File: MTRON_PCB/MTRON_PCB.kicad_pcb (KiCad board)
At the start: 2 copper layers, 48 x 50 mm, 42 parts, among them J1 Conn_01x02, J2 Conn_01x02, J3 Conn_01x02, J4 Conn_01x02, J5 Conn_01x06, J6 Conn_01x02, J7 Conn_01x03, J8 Conn_01x02, J9 Conn_01x03, U1 Teensy4.0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

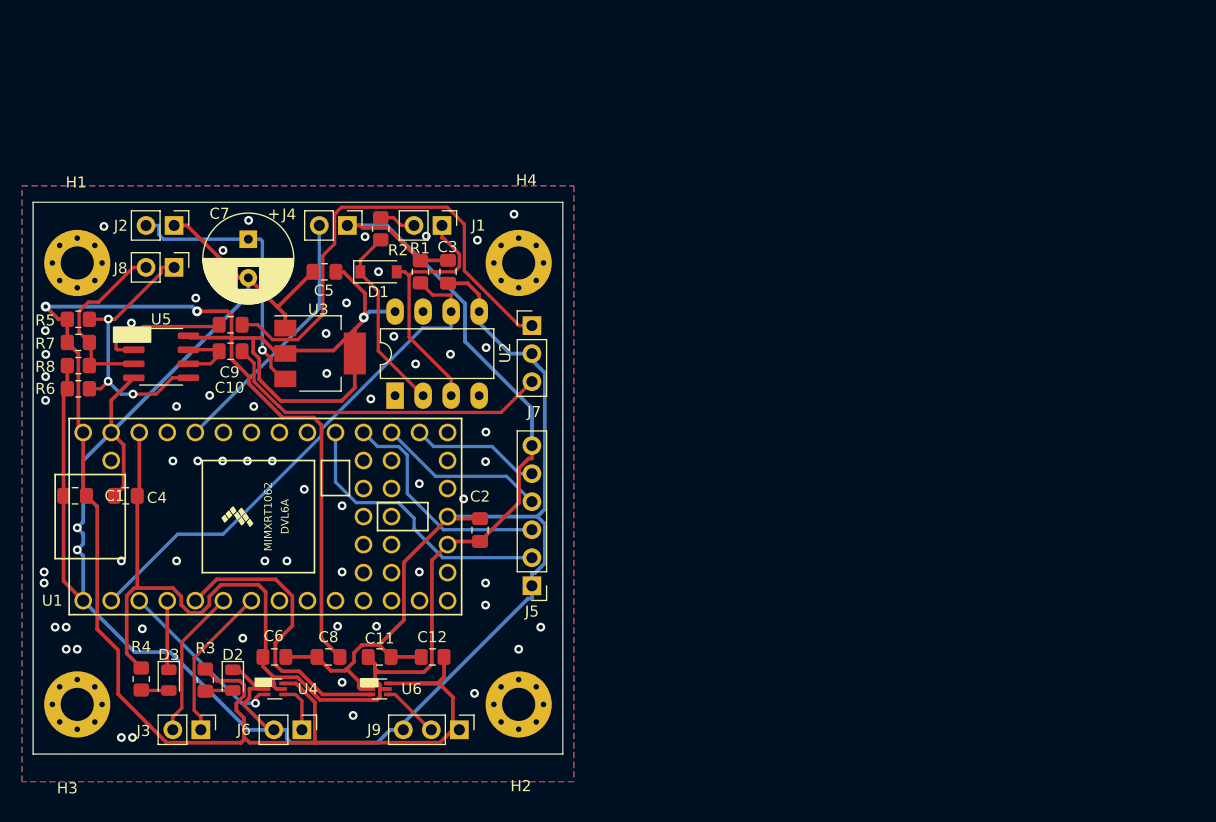
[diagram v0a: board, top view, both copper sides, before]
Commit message: update design files, new version has less parts
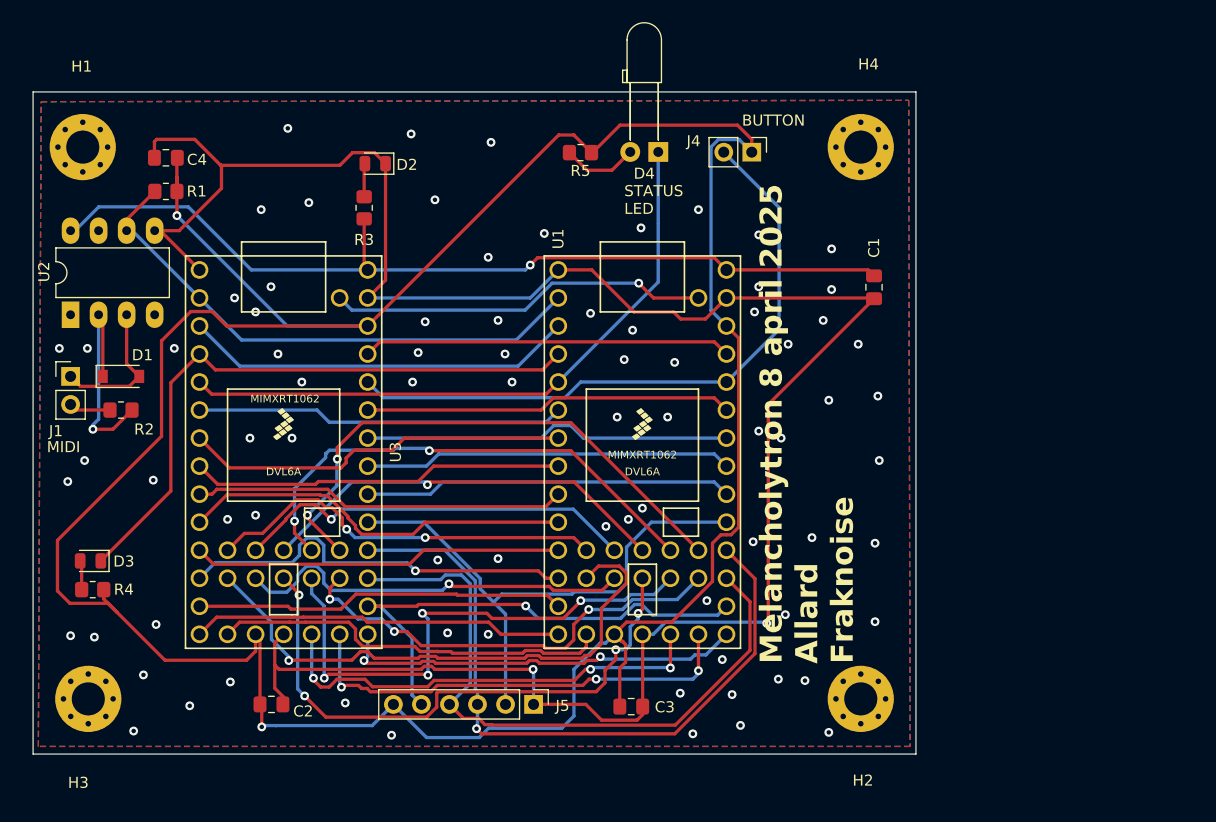
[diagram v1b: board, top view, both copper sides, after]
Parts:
- removed C10, C9: 2u2, Capacitor_SMD:C_0805_2012Metric_Pad1.18x1.45mm_HandSolder
- removed C11, C12, C5, C6, C8: 100n, Capacitor_SMD:C_0805_2012Metric_Pad1.18x1.45mm_HandSolder
- removed C7: 330uF/35V, Capacitor_THT:CP_Radial_D8.0mm_P3.50mm
- removed J2, J3, J6, J8: Conn_01x02, Connector_PinHeader_2.54mm:PinHeader_1x02_P2.54mm_Vertical
- removed J7, J9: Conn_01x03, Connector_PinHeader_2.54mm:PinHeader_1x03_P2.54mm_Vertical
- removed R6, R7, R8: 47k, Resistor_SMD:R_0805_2012Metric_Pad1.20x1.40mm_HandSolder
- removed U4, U6: SN74LVC1T45DRL, Package_TO_SOT_SMD:SOT-563
- removed U5: LM358, Package_SO:SOIC-8_3.9x4.9mm_P1.27mm
- added D4: LED, LED_THT:LED_D3.0mm_Horizontal_O6.35mm_Z6.0mm, F.Cu at (173.7, 60.9)
- R5: value 47k -> 470R
- U3: value AZ1117-5.0 -> Teensy4.0; footprint Package_TO_SOT_SMD:SOT-223-3_TabPin2 -> TeensyLibrary:Teensy40
- moved C1 74.8 mm to (193.2, 73.2), turned to -90 degrees
- moved D2 48.5 mm to (148.0, 62.0), turned to 180 degrees
- moved R5 47.9 mm to (166.6, 61.0), turned to 180 degrees
- moved R3 45.2 mm to (147.0, 66.0), turned to 90 degrees
- moved C3 42.8 mm to (171.2, 111.2), turned to 0 degrees
- moved J4 37.2 mm to (182.1, 61.0)
- moved J1 36.3 mm to (120.4, 81.3), turned to 0 degrees
- moved U1 34.7 mm to (172.2, 88.1), turned to -90 degrees
- moved H4 32.7 mm to (192.0, 60.5)
- moved H2 31.0 mm to (192.0, 110.5)
- moved C4 30.8 mm to (129.0, 61.5)
- moved U2 30.3 mm to (120.4, 75.7)
- moved R2 28.7 mm to (125.0, 84.3), turned to 0 degrees
- moved D1 25.2 mm to (125.0, 81.3)
- moved C2 24.6 mm to (138.6, 111.0), turned to 0 degrees
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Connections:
- C1 pad 1: +5V -> P33
- C1 pad 2: GND -> P1
- C2 pad 1: +3V3 -> P16
- C2 pad 2: GND -> P1
- C3 pad 1: +3V3 -> P16
- C3 pad 2: GND -> P1
- C4 pad 1: +3V3 -> P16
- C4 pad 2: GND -> P1
- D2 pad 1: GND -> P1
- J4 pad 1: +3V3 -> P16
- J4 pad 2: Net-(J4-Pin_2) -> P29
- J5 pad 1: GND -> P1
- J5 pad 2: Net-(J5-Pin_2) -> P24
- J5 pad 3: Net-(J5-Pin_3) -> P23
- J5 pad 4: Net-(J5-Pin_4) -> P22
- J5 pad 5: Net-(J5-Pin_5) -> P21
- J5 pad 6: +3V3 -> P16
- R1 pad 1: +3V3 -> P16
- R1 pad 2: Net-(U1-0_RX1_CRX2_CS1) -> P2
- R3 pad 1: +5V -> P33
- R4 pad 1: +3V3 -> P16
- R5 pad 1: +5V -> P16
- U1 pad 1: GND -> P1
- U1 pad 10: unconnected-(U1-8_TX2_IN1) -> P10
- U1 pad 11: unconnected-(U1-9_OUT1C) -> P11
- U1 pad 12: unconnected-(U1-10_CS_MQSR) -> P12
- U1 pad 13: unconnected-(U1-11_MOSI_CTX1) -> P13
- U1 pad 14: unconnected-(U1-12_MISO_MQSL) -> P14
- U1 pad 15: unconnected-(U1-VBAT) -> P15
- U1 pad 16: +3V3 -> P16
- U1 pad 17: GND -> P1
- U1 pad 18: unconnected-(U1-PROGRAM) -> P18
- U1 pad 19: unconnected-(U1-ON_OFF) -> P19
- U1 pad 2: Net-(U1-0_RX1_CRX2_CS1) -> P2
- U1 pad 20: unconnected-(U1-13_SCK_CRX1_LED) -> P20
- U1 pad 21: Net-(J5-Pin_5) -> P21
- U1 pad 22: Net-(J5-Pin_4) -> P22
- U1 pad 23: Net-(J5-Pin_3) -> P23
- U1 pad 24: Net-(J5-Pin_2) -> P24
- U1 pad 25: unconnected-(U1-18_A4_SDA0) -> P25
- U1 pad 26: unconnected-(U1-19_A5_SCL0) -> P26
- U1 pad 27: unconnected-(U1-20_A6_TX5_LRCLK1) -> P27
- U1 pad 28: unconnected-(U1-21_A7_RX5_BCLK1) -> P28
- U1 pad 29: Net-(J4-Pin_2) -> P29
- U1 pad 3: Net-(U1-1_TX1_CTX2_MISO1) -> P3
- U1 pad 30: unconnected-(U1-23_A9_CRX1_MCLK1) -> P30
- U1 pad 31: +3V3 -> P16
- U1 pad 32: GND -> P1
- U1 pad 33: +5V -> P33
- U1 pad 34: unconnected-(U1-VUSB) -> P34
- U1 pad 35: unconnected-(U1-24_A10_TX6_SCL2) -> P35
- U1 pad 36: unconnected-(U1-25_A11_RX6_SDA2) -> P36
- U1 pad 37: unconnected-(U1-26_A12_MOSI1) -> P37
- U1 pad 38: unconnected-(U1-27_A13_SCK1) -> P38
- U1 pad 39: unconnected-(U1-28_RX7) -> P39
- U1 pad 40: unconnected-(U1-29_TX7) -> P40
- U1 pad 41: unconnected-(U1-30_CRX3) -> P41
- U1 pad 42: unconnected-(U1-31_CTX3) -> P42
- U1 pad 43: unconnected-(U1-32_OUT1B) -> P43
- U1 pad 44: unconnected-(U1-33_MCLK2) -> P44
- U1 pad 6: Net-(J3-Pin_2) -> P6
- U1 pad 7: Net-(J3-Pin_1) -> P7
- U1 pad 8: unconnected-(U1-6_OUT1D) -> P8
- U1 pad 9: unconnected-(U1-7_RX2_OUT1A) -> P9
- U2 pad 5: GND -> P1
- U2 pad 6: Net-(U1-0_RX1_CRX2_CS1) -> P2
- U2 pad 8: +5V -> P33
- U3 pad 1: GND -> P1
- U3 pad 2: +5V -> P2
- U3 pad 3: Net-(J2-Pin_2) -> P3
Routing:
- net P16: track 0.00 -> 258.7 mm, vias 0 -> 2
- net GND: track 231.6 -> 0.00 mm, vias 63 -> 0
- net +5V: track 203.9 -> 0.00 mm, vias 3 -> 0
- net P1: track 0.00 -> 199.3 mm, vias 0 -> 81
- net +3V3: track 134.2 -> 0.00 mm
- net P33: track 0.00 -> 82.0 mm, vias 0 -> 1
- net P23: track 0.00 -> 63.3 mm, vias 0 -> 1
- net P22: track 0.00 -> 59.8 mm
- net P29: track 0.00 -> 58.6 mm
- net P39: track 0.00 -> 53.0 mm, vias 0 -> 4
- net P43: track 0.00 -> 51.3 mm, vias 0 -> 1
- net P24: track 0.00 -> 50.7 mm
- net P36: track 0.00 -> 50.1 mm, vias 0 -> 2
- net LD1: track 6.32 -> 56.2 mm
- net P2: track 0.00 -> 49.4 mm
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- added copper zone on B.Cu, net P1
- added copper zone on F.Cu, net P1
- removed copper zone on B.Cu, net GND
- removed copper zone on F.Cu, net GND
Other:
- board size 48 x 50 mm -> 80 x 60 mm
- board text added: "BUTTON"
- board text added: "Melancholytron 8 april 2025 Allard Fraknoise"
- board text added: "STATUS LED"
- board text removed: "+"
- board text removed: "12-6-2022"
- board text removed: "3V3"
- board text removed: "ALL RIGHTS RESERVED 2022"
- board text removed: "ANALOG INPUTS"
- board text removed: "AUDIO BUFFER INPUT"
- board text removed: "AUDIO BUFFER OUTPUT"
- board text removed: "GND"
- board text removed: "LEFT"
- board text removed: "MELANCHOLYTRON 0.1 A.Krijger J.Jessurun E.Oetelaar"
- board text removed: "MIDI OUTPUT"
- board text removed: "MISC IO"
- board text removed: "MODE SWITCH"
- board text removed: "WS2812 LEDS"

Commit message: nieuwe versie met alles THT en pull up voor switch. connector voor power. flip van linker device orientatie
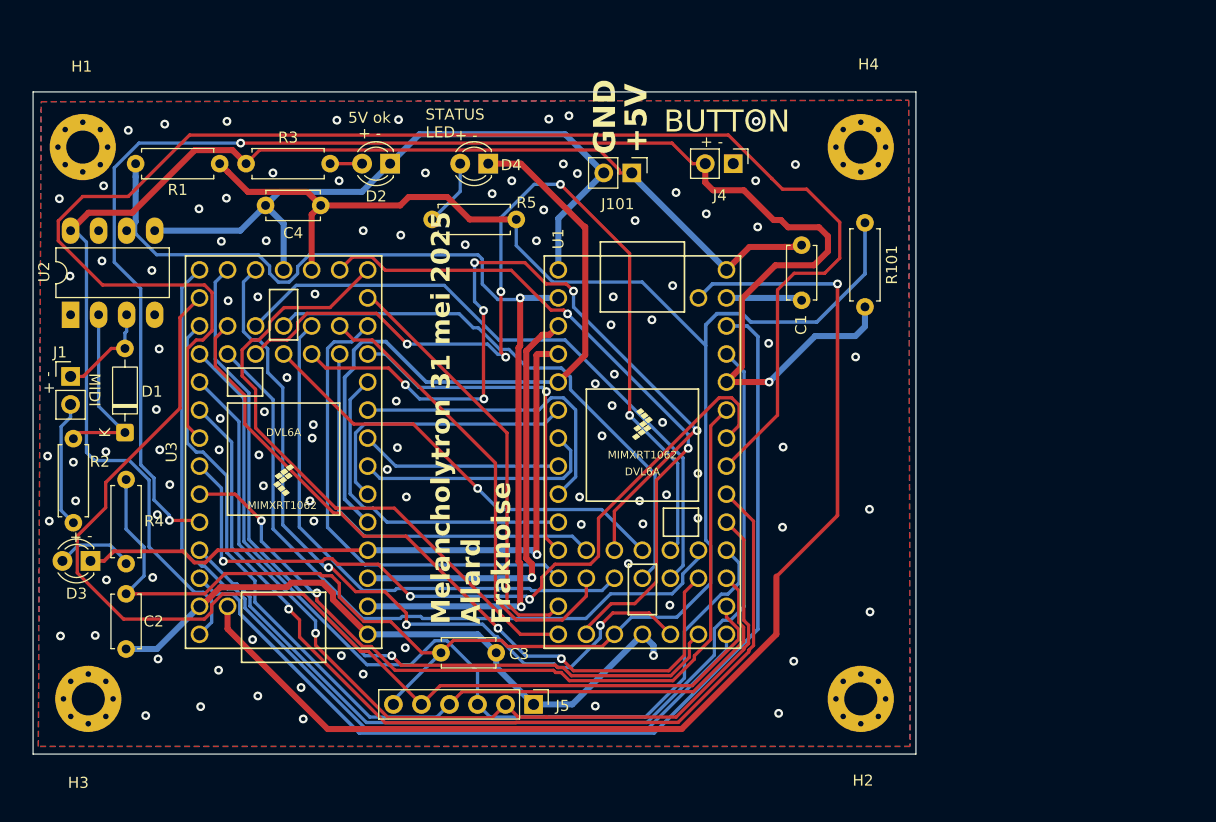
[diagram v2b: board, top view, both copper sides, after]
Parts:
- added J101: Conn_01x02, Connector_PinHeader_2.54mm:PinHeader_1x02_P2.54mm_Vertical, F.Cu at (171.3, 62.8)
- added R101: 470R, Resistor_THT:R_Axial_DIN0207_L6.3mm_D2.5mm_P7.62mm_Horizontal, F.Cu at (192.4, 75.0)
- C1, C2, C3, C4: footprint Capacitor_SMD:C_0805_2012Metric_Pad1.18x1.45mm_HandSolder -> Capacitor_THT:C_Disc_D4.7mm_W2.5mm_P5.00mm
- D1: footprint Diode_SMD:D_SOD-123 -> Diode_THT:D_DO-35_SOD27_P7.62mm_Horizontal
- D2, D3: footprint LED_SMD:LED_0805_2012Metric -> LED_THT:LED_D3.0mm
- D4: footprint LED_THT:LED_D3.0mm_Horizontal_O6.35mm_Z6.0mm -> LED_THT:LED_D3.0mm
- R1, R2, R3, R4, R5: footprint Resistor_SMD:R_0805_2012Metric_Pad1.20x1.40mm_HandSolder -> Resistor_THT:R_Axial_DIN0207_L6.3mm_D2.5mm_P7.62mm_Horizontal
- moved C3 17.9 mm to (154.0, 106.3)
- moved C2 16.6 mm to (125.4, 101.0), turned to -90 degrees
- moved D4 15.4 mm to (158.2, 62.0)
- moved C4 14.7 mm to (143.1, 65.8)
- moved R3 11.4 mm to (136.3, 62.0), turned to 0 degrees
- moved R2 11.1 mm to (120.7, 94.5), turned to 90 degrees
- moved R4 10.4 mm to (125.4, 90.6), turned to -90 degrees
- moved R5 8.40 mm to (160.8, 67.1)
- moved C1 7.59 mm to (186.6, 69.4)
- moved R1 5.49 mm to (133.9, 62.0)
- moved D1 5.10 mm to (125.3, 86.4), turned to 90 degrees
- moved J4 1.97 mm to (180.4, 62.0)
- moved D2 1.35 mm to (149.4, 62.0)
- turned U3 to 90 degrees
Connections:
- C1 pad 2: P1 -> GROUND
- C2 pad 2: P1 -> GROUND
- C3 pad 2: P1 -> GROUND
- C4 pad 2: P1 -> GROUND
- D2 pad 1: P1 -> GROUND
- J4 pad 1: P16 -> GROUND
- J5 pad 1: P1 -> GROUND
- U1 pad 1: P1 -> GROUND
- U1 pad 17: P1 -> GROUND
- U1 pad 31: P16 -> P31
- U1 pad 32: P1 -> GROUND
- U2 pad 5: P1 -> GROUND
- U3 pad 1: P1 -> GROUND
- U3 pad 17: P1 -> GROUND
- U3 pad 31: P16 -> P31
- U3 pad 32: P1 -> GROUND
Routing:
- net P1: track 199.3 -> 0.00 mm, vias 81 -> 0
- net GROUND: track 0.00 -> 129.6 mm, vias 0 -> 105
- net P26: track 33.4 -> 137.9 mm
- net P31: track 0.00 -> 90.7 mm
- net P29: track 58.6 -> 142.4 mm, vias 0 -> 3
- net P16: track 258.7 -> 184.7 mm, vias 2 -> 0
- net P34: track 34.5 -> 106.3 mm
- net P21: track 45.9 -> 102.5 mm, vias 1 -> 0
- net P25: track 33.4 -> 86.4 mm, vias 0 -> 1
- net P30: track 33.4 -> 85.6 mm
- net P20: track 37.1 -> 86.9 mm, vias 2 -> 0
- net P2: track 49.4 -> 97.0 mm, vias 0 -> 2
- net P28: track 33.4 -> 77.9 mm, vias 0 -> 2
- net P33: track 82.0 -> 124.2 mm, vias 1 -> 0
- net P27: track 33.5 -> 71.7 mm, vias 0 -> 3
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- added copper zone on B.Cu, net GROUND
- added copper zone on F.Cu, net GROUND
- removed copper zone on B.Cu, net P1
- removed copper zone on F.Cu, net P1
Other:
- board text added: "+ -"
- board text added: "+5V"
- board text added: "- +"
- board text added: "5V ok"
- board text added: "GND"
- board text added: "Melancholytron 31 mei 2025 Allard Fraknoise"
- board text removed: "Melancholytron 8 april 2025 Allard Fraknoise"

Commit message: new version, includes fix for 3v3, audio transformer, logo, based on new findings.
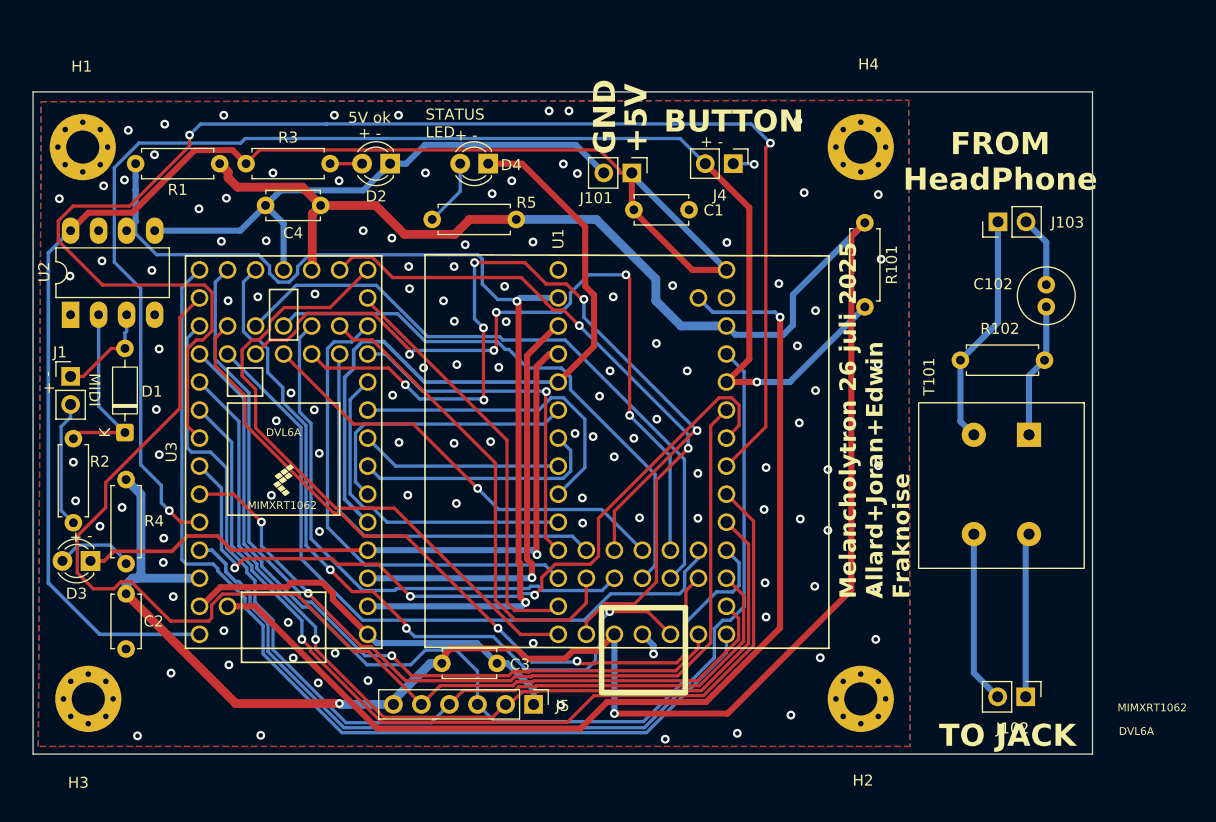
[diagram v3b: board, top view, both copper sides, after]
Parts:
- added C102: C_Small, Capacitor_THT:C_Radial_D5.0mm_H11.0mm_P2.00mm, F.Cu at (208.8, 73.0)
- added G***: LOGO, LOGO, B.Cu at (190.6, 84.4)
- added J102: Conn_01x02, Connector_PinHeader_2.54mm:PinHeader_1x02_P2.54mm_Vertical, F.Cu at (206.9, 110.3)
- added J103: Conn_01x02, Connector_PinHeader_2.54mm:PinHeader_1x02_P2.54mm_Vertical, F.Cu at (204.4, 67.3)
- added R102: 10K, Resistor_THT:R_Axial_DIN0207_L6.3mm_D2.5mm_P7.62mm_Horizontal, F.Cu at (208.7, 79.8)
- added T101: EL-11 (tinytronics), AudioTransformer_Edwin:Transformer_EL-11-tinytronics, F.Cu at (214.2, 86.6)
- U1: footprint TeensyLibrary:Teensy40 -> TeensyLibrary:Teensy40_audio_shield
- moved C1 15.5 mm to (171.4, 66.2), turned to 0 degrees
- moved C3 0.96 mm to (154.0, 107.3)
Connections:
- U1 pad 31: P31 -> P16
- U3 pad 31: P31 -> P16
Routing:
- net P31: track 90.7 -> 0.00 mm
- net GROUND: track 129.6 -> 92.5 mm, vias 105 -> 120
- net P16: track 184.7 -> 218.2 mm, vias 0 -> 2
- net Net-(J103-Pin_1): track 0.00 -> 21.2 mm
- net Net-(J102-Pin_2): track 0.00 -> 15.6 mm
- net Net-(J102-Pin_1): track 0.00 -> 14.9 mm
- net P38: track 83.5 -> 69.3 mm
- net P29: track 142.4 -> 129.6 mm, vias 3 -> 2
- net Net-(C102-Pad2): track 0.00 -> 12.2 mm
- net P34: track 106.3 -> 94.7 mm
- net P33: track 124.2 -> 131.7 mm
- net Net-(J103-Pin_2): track 0.00 -> 6.46 mm
- net P26: track 137.9 -> 133.0 mm, vias 0 -> 2
- net P20: track 86.9 -> 89.5 mm
- net P22: track 86.2 -> 88.8 mm
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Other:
- board size 80 x 60 mm -> 96 x 60 mm
- board text added: "FROM HeadPhone"
- board text added: "Melancholytron 26 juli 2025 Allard+Joran+Edwin Fraknoise"
- board text added: "TO JACK"
- board text removed: "Melancholytron 31 mei 2025 Allard Fraknoise"
